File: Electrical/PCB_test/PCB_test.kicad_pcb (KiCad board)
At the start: 2 copper layers, 90 x 70 mm, 45 parts, among them J1 Screw_Terminal_01x02

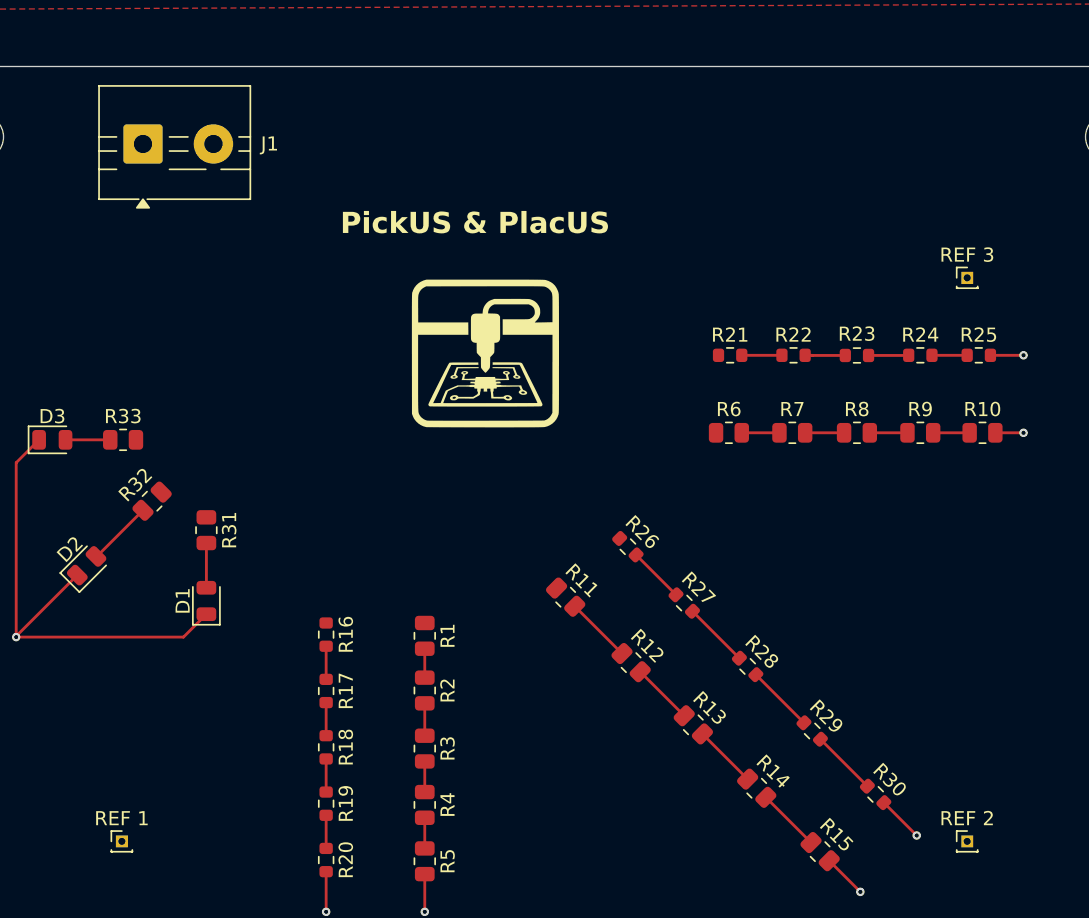
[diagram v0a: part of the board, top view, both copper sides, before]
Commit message: Position of ref now aligns on board grid
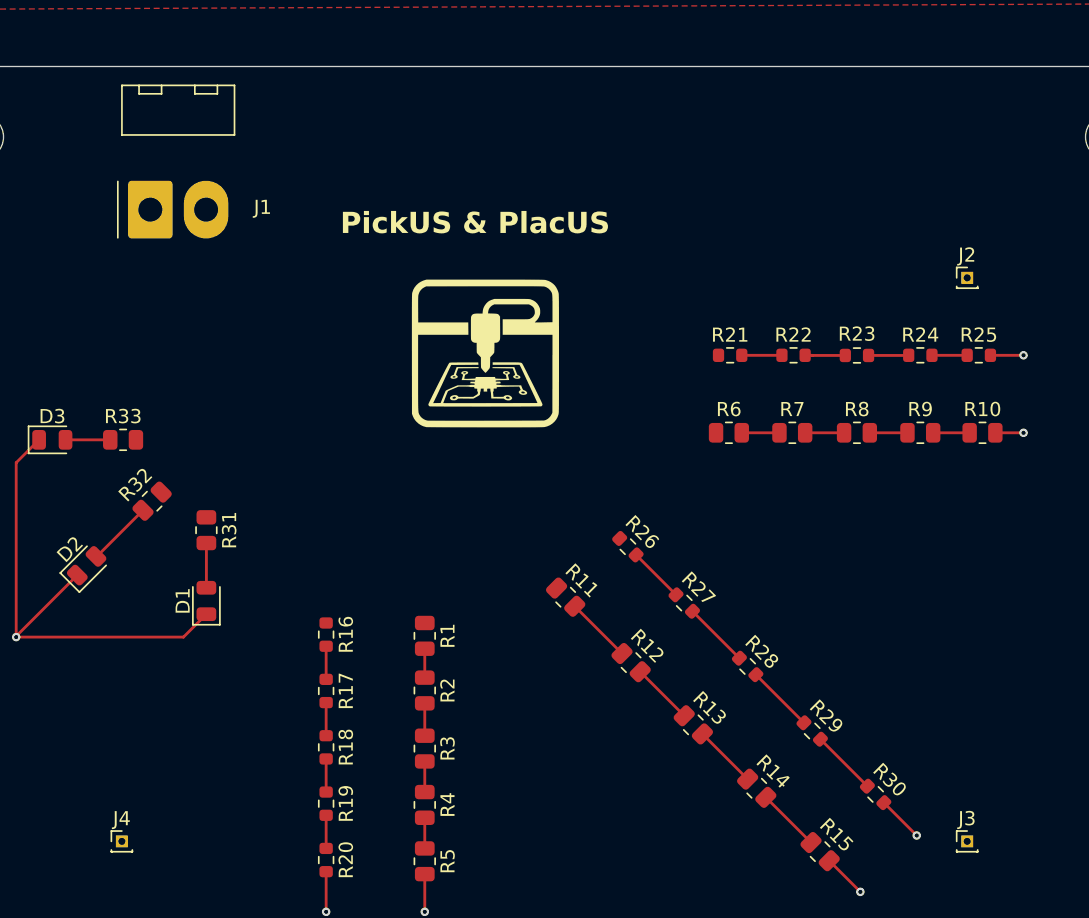
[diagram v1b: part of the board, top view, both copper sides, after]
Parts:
- J1: footprint TerminalBlock:TerminalBlock_MaiXu_MX126-5.0-02P_1x02_P5.00mm -> Connector_Molex:Molex_KK-396_A-41792-0002_1x02_P3.96mm_Horizontal
- J2: renamed from REF 3
- J3: renamed from REF 2
- J4: renamed from REF 1
- moved J1 4.69 mm to (57.0, 35.2)
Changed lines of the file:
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@@
 		(descr "Through hole straight pin header, 1x01, 1.00mm pitch, single row")
 		(tags "Through hole pin header THT 1x01 1.00mm single row")
-		(property "Reference" "REF 3"
+		(property "Reference" "J2"
 			(at 0 -1.61 0)
 			(layer "F.SilkS")
@@
 		(descr "Through hole straight pin header, 1x01, 1.00mm pitch, single row")
 		(tags "Through hole pin header THT 1x01 1.00mm single row")
-		(property "Reference" "REF 2"
+		(property "Reference" "J3"
 			(at 0 -1.61 0)
 			(layer "F.SilkS")
@@
 		(descr "Through hole straight pin header, 1x01, 1.00mm pitch, single row")
 		(tags "Through hole pin header THT 1x01 1.00mm single row")
-		(property "Reference" "REF 1"
+		(property "Reference" "J4"
 			(at 0 -1.61 0)
 			(layer "F.SilkS")
@@
 		)
 	)
-	(footprint "TerminalBlock:TerminalBlock_MaiXu_MX126-5.0-02P_1x02_P5.00mm"
+	(footprint "Connector_Molex:Molex_KK-396_A-41792-0002_1x02_P3.96mm_Horizontal"
 		(layer "F.Cu")
-		(at 56.5 30.5)
-		(descr "terminal block MaiXu MX126-5.0-02P, 2 pins, pitch 5mm, size 10.5x7.8mm, drill diameter 1.3mm, pad diameter 2.8mm, https://www.lcsc.com/datasheet/lcsc_datasheet_2309150913_MAX-MX126-5-0-03P-GN01-Cu-S-A_C5188435.pdf, script-generated using https://gitlab.com/kicad/libraries/kicad-footprint-generator/-/tree/master/scripts/TerminalBlock_MaiXu")
-		(tags "THT terminal block MaiXu MX126-5.0-02P pitch 5mm size 10.5x7.8mm drill 1.3mm pad 2.8mm")
+		(at 57.02 35.16)
+		(descr "Molex KK 396 Interconnect System, old/engineering part number: A-41792-0002 example for new part number: 26-60-5020, 2 Pins (https://www.molex.com/pdm_docs/sd/026605050_sd.pdf), generated with kicad-footprint-generator")
+		(tags "connector Molex KK-396 horizontal")
 		(property "Reference" "J1"
-			(at 9 0 0)
+			(at 7.98 -0.16 0)
 			(layer "F.SilkS")
 			(effects
@@
 		)
 		(property "Value" "Screw_Terminal_01x02"
-			(at 2.25 4.92 0)
+			(at 1.98 3.6 0)
 			(layer "F.Fab")
 			(effects
@@
 		(attr through_hole)
 		(fp_line
-			(start -3.12 -4.12)
-			(end 7.62 -4.12)
-			(stroke
-				(width 0.12)
-				(type solid)
-			)
-			(layer "F.SilkS")
-		)
-		(fp_line
-			(start -3.12 -0.5)
-			(end -1.88 -0.5)
-			(stroke
-				(width 0.12)
-				(type solid)
-			)
-			(layer "F.SilkS")
-		)
-		(fp_line
-			(start -3.12 0.5)
-			(end -1.88 0.5)
-			(stroke
-				(width 0.12)
-				(type solid)
-			)
-			(layer "F.SilkS")
-		)
-		(fp_line
-			(start -3.12 1.8)
-			(end -1.88 1.8)
+			(start -2.305001 -2)
+			(end -2.305001 2)
 			(stroke
 				(width 0.12)
@@
 		)
 		(fp_line
-			(start -3.12 3.92)
-			(end -3.12 -4.12)
+			(start -2.015 -8.82)
+			(end 5.975 -8.82)
 			(stroke
 				(width 0.12)
@@
 		)
 		(fp_line
-			(start -0.3 3.92)
-			(end -3.12 3.92)
+			(start -2.015 -5.3)
+			(end -2.015 -8.82)
 			(stroke
 				(width 0.12)
@@
 		)
 		(fp_line
-			(start 1.88 -0.5)
-			(end 3.188 -0.5)
+			(start -0.8 -8.82)
+			(end -0.8 -8.22)
 			(stroke
 				(width 0.12)
@@
 		)
 		(fp_line
-			(start 1.88 0.5)
-			(end 3.188 0.5)
+			(start -0.8 -8.22)
+			(end 0.8 -8.22)
 			(stroke
 				(width 0.12)
@@
 		)
 		(fp_line
-			(start 1.88 1.8)
-			(end 4.457 1.8)
+			(start 0.8 -8.22)
+			(end 0.8 -8.82)
 			(stroke
 				(width 0.12)
@@
 		)
 		(fp_line
-			(start 5.543 1.8)
-			(end 7.62 1.8)
+			(start 3.16 -8.82)
+			(end 3.16 -8.22)
 			(stroke
 				(width 0.12)
@@
 		)
 		(fp_line
-			(start 6.812 -0.5)
-			(end 7.62 -0.5)
+			(start 3.16 -8.22)
+			(end 4.76 -8.22)
 			(stroke
 				(width 0.12)
@@
 		)
 		(fp_line
-			(start 6.812 0.5)
-			(end 7.62 0.5)
+			(start 4.76 -8.22)
+			(end 4.76 -8.82)
 			(stroke
 				(width 0.12)
@@
 		)
 		(fp_line
-			(start 7.62 -4.12)
-			(end 7.62 3.92)
+			(start 5.975 -8.82)
+			(end 5.975 -5.3)
 			(stroke
 				(width 0.12)
@@
 		)
 		(fp_line
-			(start 7.62 3.92)
-			(end 0.3 3.92)
+			(start 5.975 -5.3)
+			(end -2.015 -5.3)
 			(stroke
 				(width 0.12)
@@
 		(fp_poly
 			(pts
-				(xy 0 3.92) (xy 0.44 4.53) (xy -0.44 4.53)
+				(xy -2.41 -9.22) (xy 6.37 -9.22) (xy 6.37 2.9) (xy -2.41 2.9)
 			)
 			(stroke
-				(width 0.12)
-				(type solid)
-			)
-			(fill yes)
-			(layer "F.SilkS")
-		)
-		(fp_rect
-			(start -3.5 -4.5)
-			(end 8 4.31)
-			(stroke
 				(width 0.05)
 				(type solid)
@@
 		)
 		(fp_line
-			(start -3 -4)
-			(end 7.5 -4)
-			(stroke
-				(width 0.1)
-				(type solid)
-			)
-			(layer "F.Fab")
-		)
-		(fp_line
-			(start -3 -0.5)
-			(end 7.5 -0.5)
-			(stroke
-				(width 0.1)
-				(type solid)
-			)
-			(layer "F.Fab")
-		)
-		(fp_line
-			(start -3 0.5)
-			(end 7.5 0.5)
-			(stroke
-				(width 0.1)
-				(type solid)
-			)
-			(layer "F.Fab")
-		)
-		(fp_line
-			(start -3 1.8)
-			(end 7.5 1.8)
-			(stroke
-				(width 0.1)
-				(type solid)
-			)
-			(layer "F.Fab")
-		)
-		(fp_line
-			(start -3 1.85)
-			(end -3 -4)
-			(stroke
-				(width 0.1)
-				(type solid)
-			)
-			(layer "F.Fab")
-		)
-		(fp_line
-			(start -1.05 3.8)
-			(end -3 1.85)
-			(stroke
-				(width 0.1)
-				(type solid)
-			)
-			(layer "F.Fab")
-		)
-		(fp_line
-			(start 1.018 -1.213)
-			(end -1.213 1.018)
+			(start -1.905 -0.5)
+			(end -1.197893 0)
 			(stroke
 				(width 0.1)
@@
 		)
 		(fp_line
-			(start 1.213 -1.018)
-			(end -1.018 1.213)
+			(start -1.905 2.4)
+			(end -1.904999 -8.71)
 			(stroke
 				(width 0.1)
@@
 		)
 		(fp_line
-			(start 6.018 -1.213)
-			(end 3.787 1.018)
+			(start -1.904999 -8.71)
+			(end 5.865 -8.71)
 			(stroke
 				(width 0.1)
@@
 		)
 		(fp_line
-			(start 6.213 -1.018)
-			(end 3.982 1.213)
+			(start -1.197893 0)
+			(end -1.905 0.5)
 			(stroke
 				(width 0.1)
@@
 		)
 		(fp_line
-			(start 7.5 -4)
-			(end 7.5 3.8)
+			(start 5.865 -8.71)
+			(end 5.865 2.4)
 			(stroke
 				(width 0.1)
@@
 		)
 		(fp_line
-			(start 7.5 3.8)
-			(end -1.05 3.8)
-			(stroke
-				(width 0.1)
-				(type solid)
-			)
-			(layer "F.Fab")
-		)
-		(fp_circle
-			(center 0 0)
-			(end 1.6 0)
+			(start 5.865 2.4)
+			(end -1.905 2.4)
 			(stroke
 				(width 0.1)
 				(type solid)
 			)
-			(fill no)
-			(layer "F.Fab")
-		)
-		(fp_circle
-			(center 5 0)
-			(end 6.6 0)
-			(stroke
-				(width 0.1)
-				(type solid)
-			)
-			(fill no)
 			(layer "F.Fab")
 		)
 		(fp_text user "${REFERENCE}"
-			(at 2.25 2.65 0)
+			(at 1.98 -8.01 0)
 			(layer "F.Fab")
 			(effects
@@
 		(pad "1" thru_hole roundrect
 			(at 0 0)
-			(size 2.8 2.8)
-			(drill 1.3)
+			(size 3.16 4.1)
+			(drill 1.7)
 			(layers "*.Cu" "*.Mask")
 			(remove_unused_layers no)
-			(roundrect_rratio 0.089286)
+			(roundrect_rratio 0.079114)
 			(net 1 "GND")
 			(pinfunction "Pin_1")
 			(pintype "passive")
 		)
-		(pad "2" thru_hole circle
-			(at 5 0)
-			(size 2.8 2.8)
-			(drill 1.3)
+		(pad "2" thru_hole oval
+			(at 3.96 0)
+			(size 3.16 4.1)
+			(drill 1.7)
 			(layers "*.Cu" "*.Mask")
 			(remove_unused_layers no)
@@
 		)
 		(embedded_fonts no)
-		(model "${KICAD9_3DMODEL_DIR}/TerminalBlock.3dshapes/TerminalBlock_MaiXu_MX126-5.0-02P_1x02_P5.00mm.step"
+		(model "${KICAD9_3DMODEL_DIR}/Connector_Molex.3dshapes/Molex_KK-396_A-41792-0002_1x02_P3.96mm_Horizontal.step"
 			(offset
 				(xyz 0 0 0)
